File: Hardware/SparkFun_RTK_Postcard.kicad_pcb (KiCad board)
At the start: 4 copper layers, 43.2 x 43.2 mm, 133 parts, among them J1 USB_C_Receptacle, J10 Conn_01x06, J2 Conn_01x05, J3 JST_2mm_LiPo, J4 Qwiic_RA, J5 SMA_Edge, J7 Qwiic_RA, J8 JST_Locking_4, J9 I2C, Q1 MBT3904DW1, SW4 Reset, SW5 Boot, U1 DT1042-04SO, U2 AP2112K-3.3, U3 LG290P, U4 CH342F, U5 ESP32-PICO-V3-02

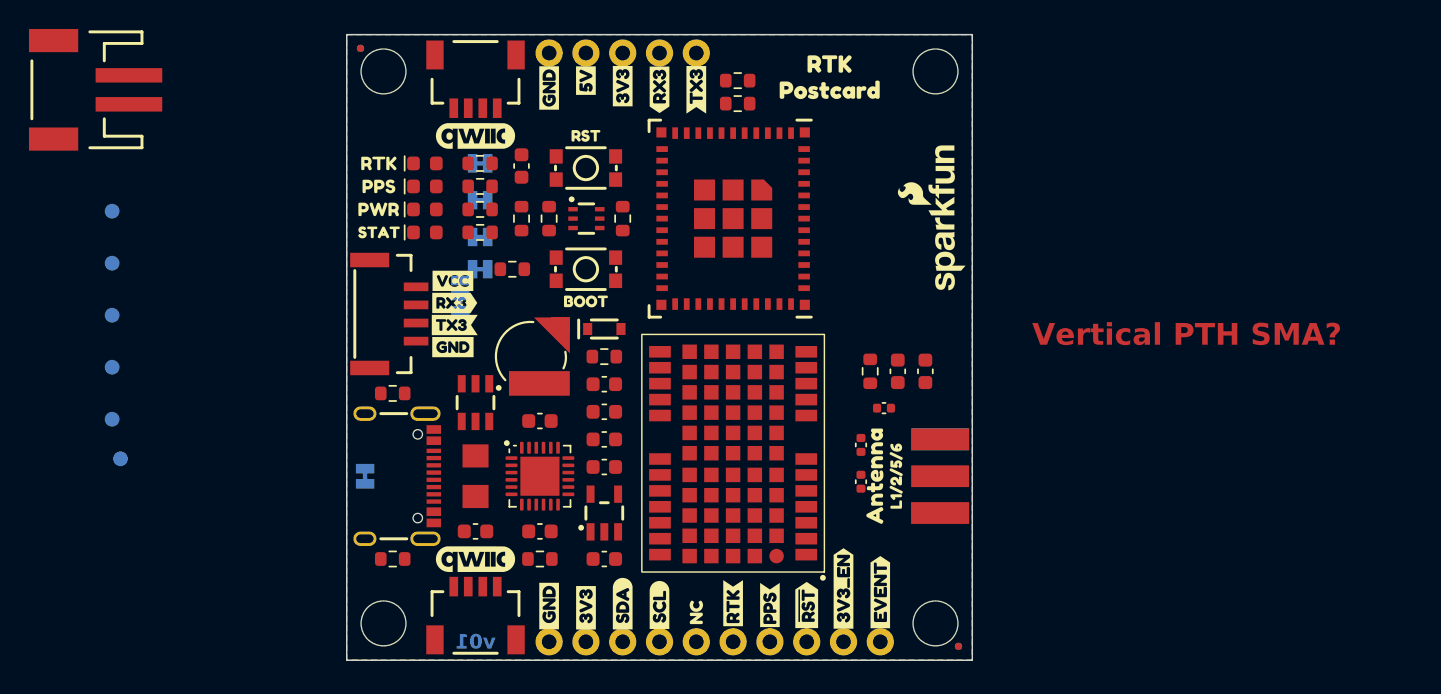
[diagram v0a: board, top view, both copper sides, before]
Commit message: Rotate silkscreen. Add AIO pin.
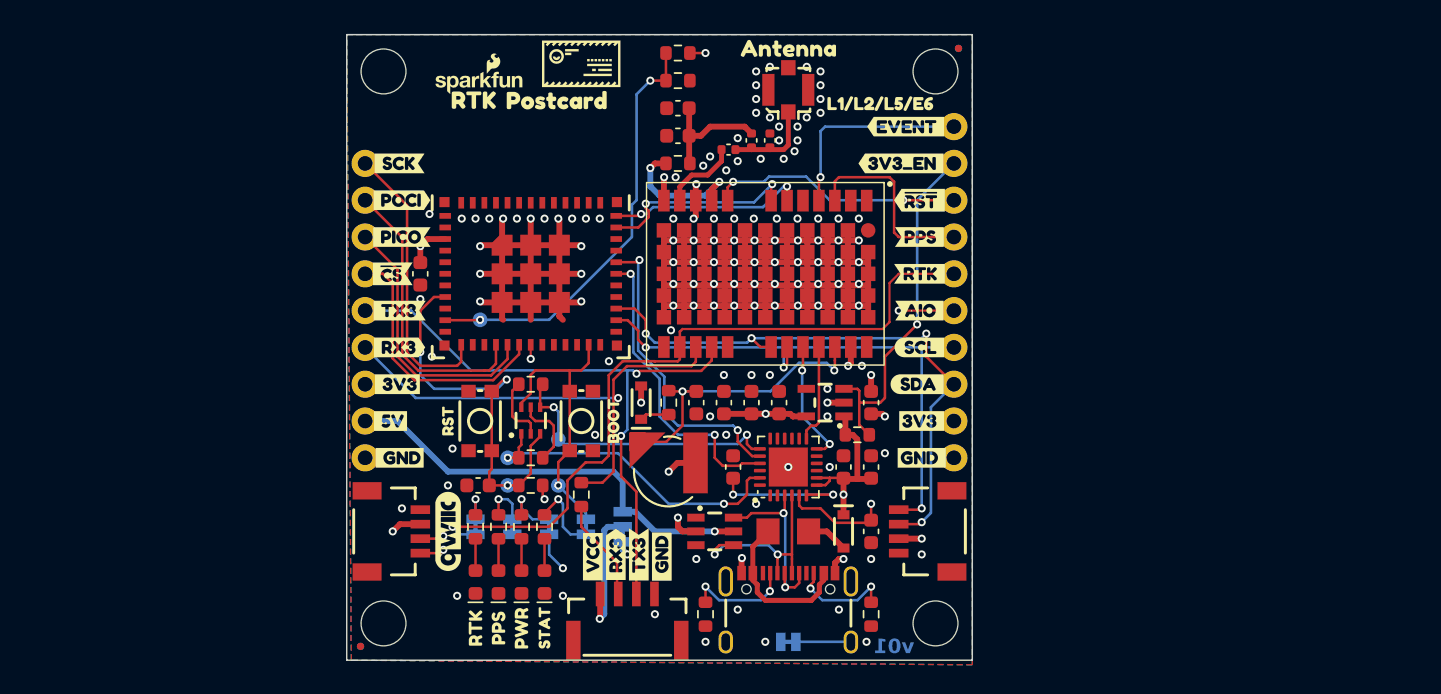
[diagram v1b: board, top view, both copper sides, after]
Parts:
- removed J5: SMA_Edge, SparkFun-Connector:SMA_Edge
- removed TP5: PTH, SparkFun-Connector:TestPoint-1.0mm
- removed kibuzzard-64C2E728: G***, kibuzzard-64C2E728
- removed kibuzzard-64CB1646: G***, kibuzzard-64CB1646
- removed kibuzzard-64CB1658: G***, kibuzzard-64CB1658
- removed kibuzzard-650880E6: G***, kibuzzard-650880E6
- removed kibuzzard-66C94943: G***, kibuzzard-66C94943
- removed kibuzzard-66C94FCB: G***, kibuzzard-66C94FCB
- removed kibuzzard-66CAA41A: G***, kibuzzard-66CAA41A
- removed kibuzzard-66CAA426 (x2): G***, kibuzzard-66CAA426
- removed kibuzzard-66CAA432 (x2): G***, kibuzzard-66CAA432
- removed kibuzzard-66CAA594: G***, kibuzzard-66CAA594
- removed kibuzzard-66CAA70F: G***, kibuzzard-66CAA70F
- removed kibuzzard-66CAA7B2: G***, kibuzzard-66CAA7B2
- removed kibuzzard-66CAA7D2: G***, kibuzzard-66CAA7D2
- removed kibuzzard-66CAA9A5 (x2): G***, kibuzzard-66CAA9A5
- removed kibuzzard-66CAA9AE (x2): G***, kibuzzard-66CAA9AE
- removed kibuzzard-66CAAA3A: G***, kibuzzard-66CAAA3A
- removed kibuzzard-66CAAA42: G***, kibuzzard-66CAAA42
- removed kibuzzard-66CB37A9 (x2): G***, kibuzzard-66CB37A9
- removed kibuzzard-66CB37CC: G***, kibuzzard-66CB37CC
- removed kibuzzard-66CB37D7: G***, kibuzzard-66CB37D7
- removed kibuzzard-66CB38B8: G***, kibuzzard-66CB38B8
- removed kibuzzard-66CB38C4: G***, kibuzzard-66CB38C4
- removed kibuzzard-66CB39E1 (x2): G***, kibuzzard-66CB39E1
- removed kibuzzard-66CB3B6E: G***, kibuzzard-66CB3B6E
- removed kibuzzard-66CB3B7A: G***, kibuzzard-66CB3B7A
- removed kibuzzard-66CB3BAB: G***, kibuzzard-66CB3BAB
- removed kibuzzard-66CB3BB4: G***, kibuzzard-66CB3BB4
- removed kibuzzard-66CB3BBD: G***, kibuzzard-66CB3BBD
- removed kibuzzard-66CB3BC8: G***, kibuzzard-66CB3BC8
- removed kibuzzard-66CB3BD0: G***, kibuzzard-66CB3BD0
- removed kibuzzard-66CB3BFF: G***, kibuzzard-66CB3BFF
- removed kibuzzard-66CB3C14: G***, kibuzzard-66CB3C14
- removed kibuzzard-66CBD5AE: G***, kibuzzard-66CBD5AE
- removed kibuzzard-66E5026E: G***, kibuzzard-66E5026E
- removed kibuzzard-66E50275: G***, kibuzzard-66E50275
- added C12: 1.0uF, SparkFun-Capacitor:C_0603_1608Metric, F.Cu at (140.3, 90.8)
- added D7: PESD0603-240, SparkFun-Capacitor:C_0603_1608Metric, F.Cu at (171.4, 99.7)
- added D8: BAT60A, SparkFun-Semiconductor-Standard:SOD-323, F.Cu at (169.5, 108.6)
- added J6: U.FL, SparkFun-Connector:U.FL, F.Cu at (165.7, 78.1)
- added kibuzzard-66F2CCE8: G***, kibuzzard-66F2CCE8, B.Cu at (151.8, 111.6)
- added kibuzzard-66F2CD12: G***, kibuzzard-66F2CD12, B.Cu at (149.2, 111.4)
- added kibuzzard-66F2CD24: G***, kibuzzard-66F2CD24, B.Cu at (144.1, 111.3)
- added kibuzzard-66F2CD30: G***, kibuzzard-66F2CD30, B.Cu at (146.7, 111.1)
- added kibuzzard-66F317F0: G***, kibuzzard-66F317F0, F.Cu at (174.6, 98.4)
- added kibuzzard-66F31834: G***, kibuzzard-66F31834, F.Cu at (173.8, 80.6)
- added kibuzzard-66F3184B: G***, kibuzzard-66F3184B, F.Cu at (173.5, 83.2)
- added kibuzzard-66F3185F: G***, kibuzzard-66F3185F, F.Cu at (174.8, 85.7)
- added kibuzzard-66F3186F: G***, kibuzzard-66F3186F, F.Cu at (174.8, 88.3)
- added kibuzzard-66F3187E: G***, kibuzzard-66F3187E, F.Cu at (174.8, 90.8)
- added kibuzzard-66F3188A: G***, kibuzzard-66F3188A, F.Cu at (174.8, 95.9)
- added kibuzzard-66F318A4: G***, kibuzzard-66F318A4, F.Cu at (174.9, 101.0)
- added kibuzzard-66F318AF: G***, kibuzzard-66F318AF, F.Cu at (174.9, 103.5)
- added kibuzzard-66F318EE: G***, kibuzzard-66F318EE, F.Cu at (138.9, 83.2)
- added kibuzzard-66F3190E: G***, kibuzzard-66F3190E, F.Cu at (139.1, 85.7)
- added kibuzzard-66F31920: G***, kibuzzard-66F31920, F.Cu at (139.1, 88.3)
- added kibuzzard-66F31933: G***, kibuzzard-66F31933, F.Cu at (138.4, 90.8)
- added kibuzzard-66F3194C: G***, kibuzzard-66F3194C, F.Cu at (155.4, 110.2)
- added kibuzzard-66F3194C: G***, kibuzzard-66F3194C, F.Cu at (138.9, 93.3)
- added kibuzzard-66F31954: G***, kibuzzard-66F31954, F.Cu at (138.9, 95.9)
- added kibuzzard-66F31954: G***, kibuzzard-66F31954, F.Cu at (153.8, 110.2)
- added kibuzzard-66F31959: G***, kibuzzard-66F31959, F.Cu at (138.7, 98.4)
- added kibuzzard-66F31960: G***, kibuzzard-66F31960, F.Cu at (138.3, 101.0)
- added kibuzzard-66F31965: G***, kibuzzard-66F31965, F.Cu at (157.0, 110.3)
- added kibuzzard-66F31965: G***, kibuzzard-66F31965, F.Cu at (138.9, 103.5)
- added kibuzzard-66F31A0F: G***, kibuzzard-66F31A0F, B.Cu at (138.9, 83.2)
- added kibuzzard-66F31A40: G***, kibuzzard-66F31A40, B.Cu at (139.2, 85.7)
- added kibuzzard-66F31A48: G***, kibuzzard-66F31A48, B.Cu at (139.2, 88.4)
- added kibuzzard-66F31A50: G***, kibuzzard-66F31A50, B.Cu at (138.6, 90.8)
- added kibuzzard-66F31A58: G***, kibuzzard-66F31A58, B.Cu at (138.9, 93.3)
- added kibuzzard-66F31A60: G***, kibuzzard-66F31A60, B.Cu at (138.9, 95.9)
- added kibuzzard-66F31A68: G***, kibuzzard-66F31A68, B.Cu at (138.7, 98.4)
- added kibuzzard-66F31A71: G***, kibuzzard-66F31A71, B.Cu at (138.3, 101.0)
- added kibuzzard-66F31A78: G***, kibuzzard-66F31A78, B.Cu at (138.9, 103.5)
- added kibuzzard-66F31AC6: G***, kibuzzard-66F31AC6, B.Cu at (156.8, 95.9)
- added kibuzzard-66F31AD0: G***, kibuzzard-66F31AD0, B.Cu at (156.8, 98.7)
- added kibuzzard-66F31AE7: G***, kibuzzard-66F31AE7, B.Cu at (173.8, 80.6)
- added kibuzzard-66F31B16: G***, kibuzzard-66F31B16, B.Cu at (173.5, 83.3)
- added kibuzzard-66F31B25: G***, kibuzzard-66F31B25, B.Cu at (174.8, 85.7)
- added kibuzzard-66F31B2D: G***, kibuzzard-66F31B2D, B.Cu at (174.8, 88.3)
- added kibuzzard-66F31B33: G***, kibuzzard-66F31B33, B.Cu at (174.8, 90.8)
- added kibuzzard-66F31B4A: G***, kibuzzard-66F31B4A, B.Cu at (174.9, 101.0)
- added kibuzzard-66F31B4F: G***, kibuzzard-66F31B4F, B.Cu at (174.9, 103.5)
- added kibuzzard-66F31B5D: G***, kibuzzard-66F31B5D, B.Cu at (174.6, 98.4)
- added kibuzzard-66F31B67: G***, kibuzzard-66F31B67, B.Cu at (174.8, 95.9)
- added kibuzzard-66F31D00: G***, kibuzzard-66F31D00, F.Cu at (152.2, 110.3)
- added kibuzzard-66F3418A: G***, kibuzzard-66F3418A, F.Cu at (172.1, 79.1)
- added kibuzzard-66F3756F: G***, kibuzzard-66F3756F, F.Cu at (174.8, 93.3)
- added kibuzzard-66F37583: G***, kibuzzard-66F37583, B.Cu at (174.8, 93.3)
- G***: footprint SparkFun-Aesthetic:SparkFun_Logo_10mm -> SparkFun-Aesthetic:SparkFun_Logo_6mm
- G***: moved to B.Cu
- J3: value JST_2mm_LiPo -> Conn_01x04; footprint SparkFun-Connector:JST_SMD_2.0mm-2 -> SparkFun-Connector:1x04
- moved FID1 41.3 mm to (177.5, 75.2), turned to -90 degrees
- moved FID2 41.3 mm to (136.2, 116.5), turned to -90 degrees
- moved FID3 41.3 mm to (136.2, 116.5), turned to 90 degrees
- moved FID4 41.3 mm to (177.5, 75.2), turned to 90 degrees
- moved ST1 38.1 mm to (137.8, 76.8), turned to 90 degrees
- moved ST4 38.1 mm to (175.9, 114.9), turned to 90 degrees
- moved ST2 38.1 mm to (175.9, 76.8), turned to 90 degrees
- moved ST3 38.1 mm to (137.8, 114.9), turned to 90 degrees
- moved TP1 34.6 mm to (149.9, 102.2), turned to -90 degrees
- moved G*** 33.5 mm to (144.3, 77.5), turned to 0 degrees
- moved R1 33.2 mm to (171.4, 114.3), turned to -90 degrees
- moved kibuzzard-64C2E6D6 32.8 mm to (144.1, 115.3), turned to 90 degrees
- moved TP4 31.9 mm to (149.9, 105.4), turned to -90 degrees
- moved Ref** 31.7 mm to (138.4, 108.6)
- moved kibuzzard-64C2E6BD 31.6 mm to (145.7, 115.3), turned to 90 degrees
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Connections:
- F1 pad 2: 5V -> Net-(D8-PadA)
- J10 pad 1: unconnected-(J10-Pin_1-Pad1) -> ESP14/AIO
- J3 pad 1: unconnected-(J3---Pad1) -> SHLD_SCK
- J3 pad 2: unconnected-(J3-+-Pad2) -> SHLD_POCI
- U4 pad 11: CH342-~{RTS} -> unconnected-(U4-~{RTS1}-Pad11)
- U4 pad 12: ESP1/TX -> LG-TXD1
- U4 pad 13: ESP3/RX -> LG-RXD1
- U4 pad 15: CH342-~{DTR} -> unconnected-(U4-~{DTR1}-Pad15)
- U4 pad 19: unconnected-(U4-~{RTS0}-Pad19) -> CH342-~{RTS}
- U4 pad 20: LG-TXD1 -> ESP1/TX
- U4 pad 21: LG-RXD1 -> ESP3/RX
- U4 pad 23: unconnected-(U4-~{DTR0}-Pad23) -> CH342-~{DTR}
- U5 pad 12: unconnected-(U5-IOA32-Pad12) -> SHLD_SCK
- U5 pad 15: unconnected-(U5-IOA25-Pad15) -> SHLD_POCI
- U5 pad 16: unconnected-(U5-IOA26-Pad16) -> SHLD_PICO
- U5 pad 17: unconnected-(U5-IOA27-Pad17) -> SHLD_~{CS}
- U5 pad 18: unconnected-(U5-IOA14-Pad18) -> ESP14/AIO
- U5 pad 19: ESP12 -> unconnected-(U5-IOA12-Pad19)
- U5 pad 21: ESP15 -> unconnected-(U5-IOA15-Pad21)
- U5 pad 22: ESP2 -> unconnected-(U5-IOA2-Pad22)
- U5 pad 26: unconnected-(U5-IO20-Pad26) -> SCL
- U5 pad 27: unconnected-(U5-IO7-Pad27) -> SDA
- U5 pad 29: ESP5 -> unconnected-(U5-IO5-Pad29)
- U5 pad 34: unconnected-(U5-IO22-Pad34) -> LG-RXD2
- U5 pad 35: unconnected-(U5-IO21-Pad35) -> LG-TXD2
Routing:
- net GND: track 0.00 -> 175.9 mm, vias 0 -> 132
- net SCL: track 0.00 -> 78.1 mm, vias 0 -> 4
- net SDA: track 0.00 -> 76.5 mm, vias 0 -> 5
- net 5V: track 0.00 -> 53.4 mm, vias 0 -> 2
- net LG-RTK: track 0.00 -> 50.7 mm, vias 0 -> 1
- net LG-TXD3: track 0.00 -> 43.2 mm, vias 0 -> 2
- net LG-RXD3: track 0.00 -> 35.3 mm, vias 0 -> 1
- net ESP14/AIO: track 0.00 -> 32.1 mm, vias 0 -> 2
- net ESP35/DeviceSense: track 0.00 -> 29.6 mm, vias 0 -> 2
- net 3.3V: track 0.00 -> 29.4 mm, vias 0 -> 12
- net ESP_~{RESET}: track 0.00 -> 27.3 mm, vias 0 -> 3
- net 3V3_EN: track 0.00 -> 24.5 mm, vias 0 -> 1
- net CH342-~{DTR}: track 0.00 -> 22.8 mm, vias 0 -> 2
- net ESP1/TX: track 0.00 -> 21.3 mm, vias 0 -> 2
- net ESP3/RX: track 0.00 -> 21.0 mm, vias 0 -> 2
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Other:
- board text added: "Controlled Impedance: JLC04081H-7628 Stackup"
- board text added: "Layers: 4"
- board text added: "Thickness: 0.8mm"
- board text removed: "Controlled Impedance: JLC7628"
- board text removed: "Layers: 2"
- board text removed: "Thickness: 1.6mm"
- board text removed: "Vertical PTH SMA?"

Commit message: Fix PPS. Add SMA. Change to 1.6mm. Add BT LED. Add I2C bus. Connect RST to LG290P..
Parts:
- removed C13: 0.1uF, SparkFun-Capacitor:C_0603_1608Metric
- removed J10: Conn_01x06, SparkFun-Connector:1x06
- removed J3: Conn_01x04, SparkFun-Connector:1x04
- removed J9: I2C, SparkFun-Connector:1x04
- removed kibuzzard-66F317F0: G***, kibuzzard-66F317F0
- removed kibuzzard-66F31834: G***, kibuzzard-66F31834
- removed kibuzzard-66F3184B: G***, kibuzzard-66F3184B
- removed kibuzzard-66F3188A: G***, kibuzzard-66F3188A
- removed kibuzzard-66F31B5D: G***, kibuzzard-66F31B5D
- removed kibuzzard-66F31B67: G***, kibuzzard-66F31B67
- removed kibuzzard-66F3418A: G***, kibuzzard-66F3418A
- added D9: Blue, SparkFun-LED:LED_0603_1608Metric_Blue, F.Cu at (142.6, 112.1)
- added J11: 1x10, SparkFun-Connector:1x10, F.Cu at (177.2, 80.6)
- added J5: 1x09, SparkFun-Connector:1x09, F.Cu at (136.5, 103.5)
- added JP1: BT, SparkFun-Jumper:Jumper_2_NC_Trace, B.Cu at (141.6, 108.3)
- added JP6: I²C-EXT, SparkFun-Jumper:Jumper_3_NC-2_Trace, B.Cu at (171.0, 108.6)
- added R16: 2.2k, SparkFun-Resistor:R_0603_1608Metric, F.Cu at (142.6, 108.3)
- added R17: 2.2k, SparkFun-Resistor:R_0603_1608Metric, F.Cu at (171.4, 108.9)
- added R18: 2.2k, SparkFun-Resistor:R_0603_1608Metric, F.Cu at (169.5, 108.9)
- added R19: 0, SparkFun-Resistor:R_0402_1005Metric, F.Cu at (165.7, 80.5)
- added R20: 0, SparkFun-Resistor:R_0402_1005Metric, F.Cu at (166.4, 81.9)
- added kibuzzard-6724512A: G***, kibuzzard-6724512A, F.Cu at (142.6, 115.3)
- added kibuzzard-672EE142: G***, kibuzzard-672EE142, F.Cu at (174.3, 95.9)
- added kibuzzard-672EE156: G***, kibuzzard-672EE156, F.Cu at (174.1, 98.4)
- added kibuzzard-672FC5C6: G***, kibuzzard-672FC5C6, F.Cu at (171.4, 76.2)
- added kibuzzard-672FC5CC: G***, kibuzzard-672FC5CC, F.Cu at (171.4, 77.5)
- added kibuzzard-672FC6B5: G***, kibuzzard-672FC6B5, B.Cu at (141.6, 110.8)
- added kibuzzard-672FC715: G***, kibuzzard-672FC715, B.Cu at (166.4, 108.6)
- added kibuzzard-672FC890: G***, kibuzzard-672FC890, B.Cu at (174.5, 95.9)
- added kibuzzard-672FC894: G***, kibuzzard-672FC894, B.Cu at (174.3, 98.4)
- J2: value Conn_01x05 -> SMA_Edge; footprint SparkFun-Connector:1x05 -> SparkFun-Connector:SMA_Edge
- J6: value U.FL -> Val**
- R9: value 10k -> 100k
- U2: value AP2112K-3.3 -> RT9080-3.3
- moved J2 33.7 mm to (165.7, 76.5), turned to 0 degrees
- moved G*** 31.4 mm to (173.1, 114.3)
- moved kibuzzard-64C2EB16 7.93 mm to (172.7, 79.0)
- moved J6 6.35 mm to (170.8, 81.9), turned to 180 degrees
- moved G*** 2.54 mm to (175.1, 106.0)
- moved D8 2.27 mm to (170.5, 106.5), turned to 180 degrees
- moved kibuzzard-66F3194C 1.59 mm to (153.8, 110.2)
- moved kibuzzard-66F31954 1.59 mm to (155.4, 110.2)
- moved Ref** 0.48 mm to (138.0, 108.6)
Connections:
- C7 pad 1: 5V -> VBUS
- D8 pad A: Net-(D8-PadA) -> VBUS
- F1 pad 2: Net-(D8-PadA) -> VBUS
- J2 pad 1: LG-TXD3 -> Net-(J2-In)
- J2 pad 2: LG-RXD3 -> GND
- J4 pad 3: SDA -> SDA_1
- J4 pad 4: SCL -> SCL_1
- J6 pad 1: Net-(D3-A2) -> Net-(J6-In)
- J7 pad 3: SDA -> SDA_1
- J7 pad 4: SCL -> SCL_1
- J8 pad 2: Net-(J8-Pin_2) -> LG-TXD3
- J8 pad 3: LG-TXD3 -> Net-(J8-Pin_3)
- JP3 pad 2: PPS -> LG-PPS
- R8 pad 2: Net-(J8-Pin_2) -> Net-(J8-Pin_3)
- U3 pad 18: SDA -> SDA_0
- U3 pad 19: SCL -> SCL_0
- U4 pad 7: 5V -> VBUS
- U4 pad 8: 5V -> VBUS
- U5 pad 13: unconnected-(U5-IOA33-Pad13) -> LG-~{RESET}
- U5 pad 20: unconnected-(U5-IOA13-Pad20) -> SDA_1
- U5 pad 24: unconnected-(U5-IOA4-Pad24) -> BT_STATUS
- U5 pad 26: SCL -> SCL_0
- U5 pad 27: SDA -> SDA_0
- U5 pad 28: unconnected-(U5-IO8-Pad28) -> LG-PPS
- U5 pad 33: unconnected-(U5-IO19-Pad33) -> SCL_1
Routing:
- net SCL_1: track 0.00 -> 81.5 mm, vias 0 -> 3
- net SCL: track 78.1 -> 0.00 mm, vias 4 -> 0
- net SDA: track 76.5 -> 0.00 mm, vias 5 -> 0
- net SDA_1: track 0.00 -> 69.5 mm, vias 0 -> 4
- net LG-PPS: track 13.4 -> 67.1 mm, vias 0 -> 3
- net LG-~{RESET}: track 17.6 -> 47.2 mm, vias 2 -> 3
- net SDA_0: track 0.00 -> 29.1 mm, vias 0 -> 3
- net SCL_0: track 0.00 -> 27.4 mm, vias 0 -> 2
- net BT_STATUS: track 0.00 -> 25.8 mm, vias 0 -> 2
- net Net-(J8-Pin_3): track 0.00 -> 14.0 mm
- net VBUS: track 0.00 -> 7.90 mm
- net 3.3V: track 29.4 -> 37.3 mm
- net Net-(J8-Pin_2): track 6.84 -> 0.00 mm
- net Net-(JP6-A): track 0.00 -> 4.75 mm, vias 0 -> 1
- net 5V: track 53.4 -> 49.8 mm
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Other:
- board text added: "Controlled Impedance: JLC04161H-7628 Stackup"
- board text added: "Thickness: 1.6mm"
- board text added: "v10"
- board text removed: "Controlled Impedance: JLC04081H-7628 Stackup"
- board text removed: "Thickness: 0.8mm"
- board text removed: "v01"

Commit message: Add panel files
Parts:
- removed kibuzzard-66F31959: G***, kibuzzard-66F31959
- removed kibuzzard-66F31A68: G***, kibuzzard-66F31A68
- added kibuzzard-673B9839: G***, kibuzzard-673B9839, F.Cu at (138.4, 98.4)
- added kibuzzard-673B9839: G***, kibuzzard-673B9839, B.Cu at (138.4, 98.4)
- J11: value 1x10 -> Val**
- J5: value 1x09 -> Val**
- J6: value Val** -> U.FL
- moved kibuzzard-66CB829C 0.16 mm to (156.1, 108.3)
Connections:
- U5 pad 28: LG-PPS -> LG-EVENT
- U5 pad 4: unconnected-(U5-IA36-Pad4) -> LG-PPS
- U5 pad 9: unconnected-(U5-IA34-Pad9) -> LG-RTK
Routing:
- net LG-EVENT: track 12.3 -> 42.3 mm, vias 1 -> 3
- net GND: track 177.0 -> 205.5 mm, vias 134 -> 136
- net LG-PPS: track 67.1 -> 83.4 mm, vias 3 -> 4
- net LG-RTK: track 49.8 -> 64.8 mm, vias 1 -> 3
- net ESP_~{RESET}: track 27.3 -> 24.8 mm
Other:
- rule pad_to_mask_clearance: 0 -> 0.05

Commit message: Update sch/pcb with smaller sch parts. Update prod panel with 10% paste reduction.
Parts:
- J11: value Val** -> 1x10
- J5: value Val** -> 1x09
- JP7: value ~ -> SHLD
- turned F1 to 180 degrees
- turned R1 to 90 degrees
- turned R10 to 0 degrees
- turned R11 to 180 degrees
- turned R12 to 180 degrees
- turned R13 to 0 degrees
- turned R14 to 90 degrees
- turned R15 to 0 degrees
- turned R16 to 90 degrees
- turned R17 to -90 degrees
- turned R18 to -90 degrees
- turned R19 to 90 degrees
- turned R2 to 90 degrees
- turned R20 to 0 degrees
- turned R3 to 90 degrees
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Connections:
- F1 pad 1: Net-(F1-Pad1) -> VBUS
- F1 pad 2: VBUS -> Net-(F1-Pad2)
- J1 pad VBUS: Net-(F1-Pad1) -> Net-(F1-Pad2)
- JP6 pad 3: Net-(JP6-B) -> Net-(JP6-C)
- R1 pad 1: Net-(J1-CC2) -> GND
- R1 pad 2: GND -> Net-(J1-CC2)
- R10 pad 1: Net-(Q1B-B2) -> CH342-~{DTR}
- R10 pad 2: CH342-~{DTR} -> Net-(Q1B-B2)
- R11 pad 1: Net-(Q1A-B1) -> CH342-~{RTS}
- R11 pad 2: CH342-~{RTS} -> Net-(Q1A-B1)
- R12 pad 1: ESP35/DeviceSense -> GND
- R12 pad 2: GND -> ESP35/DeviceSense
- R13 pad 1: 3.3V -> ESP_~{RESET}
- R13 pad 2: ESP_~{RESET} -> 3.3V
- R14 pad 1: Net-(JP8-A) -> Net-(D6-A)
- R14 pad 2: Net-(D6-A) -> Net-(JP8-A)
- R15 pad 1: 3.3V -> ESP35/DeviceSense
- R15 pad 2: ESP35/DeviceSense -> 3.3V
- R16 pad 1: Net-(JP1-A) -> Net-(D9-A)
- R16 pad 2: Net-(D9-A) -> Net-(JP1-A)
- R17 pad 1: Net-(JP6-B) -> SDA_1
- R17 pad 2: SDA_1 -> Net-(JP6-C)
- R18 pad 1: Net-(JP6-A) -> SCL_1
- R18 pad 2: SCL_1 -> Net-(JP6-A)
- R19 pad 1: Net-(J2-In) -> Net-(D3-A2)
- R19 pad 2: Net-(D3-A2) -> Net-(J2-In)
- R2 pad 1: Net-(J1-CC1) -> GND
- R2 pad 2: GND -> Net-(J1-CC1)
- R20 pad 1: Net-(J6-In) -> Net-(D3-A2)
- R20 pad 2: Net-(D3-A2) -> Net-(J6-In)
- R3 pad 1: Net-(JP5-A) -> Net-(D2-A)
- R3 pad 2: Net-(D2-A) -> Net-(JP5-A)
- R4 pad 1: Net-(JP2-A) -> Net-(D1-A)
- R4 pad 2: Net-(D1-A) -> Net-(JP2-A)
- R5 pad 1: Net-(JP3-A) -> Net-(D4-A)
- R5 pad 2: Net-(D4-A) -> Net-(JP3-A)
- R6 pad 1: VCC_RF -> Net-(C3-Pad1)
- R6 pad 2: Net-(C3-Pad1) -> VCC_RF
- R7 pad 1: Net-(D5-PadC) -> V_BCKP
- R7 pad 2: V_BCKP -> Net-(D5-K)
- R8 pad 1: LG-RXD3 -> Net-(J8-Pin_3)
- R8 pad 2: Net-(J8-Pin_3) -> LG-RXD3
- R9 pad 1: 5V -> 3V3_EN
- R9 pad 2: 3V3_EN -> 5V
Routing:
- net Net-(F1-Pad2): track 0.00 -> 11.0 mm
- net Net-(F1-Pad1): track 11.0 -> 0.00 mm
- net Net-(JP6-C): track 0.00 -> 3.28 mm, vias 0 -> 1
- net Net-(JP6-B): track 3.28 -> 0.00 mm, vias 1 -> 0
- net Net-(D5-PadC): track 2.04 -> 0.00 mm
- net Net-(D5-K): track 0.00 -> 2.04 mm
